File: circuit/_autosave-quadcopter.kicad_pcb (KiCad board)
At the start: 4 copper layers, 37.7 x 37.7 mm, 112 parts, among them J1 Conn_01x01_Female, J10 Conn_01x01_Female, J11 Conn_01x01_Female, J12 Conn_01x01_Female, J13 Conn_01x01_Female, J14 Conn_01x01_Female, J15 Conn_01x01_Female, J16 Conn_01x01_Female, J17 Conn_01x01_Female, J18 USB_C_Receptacle_USB2.0, J19 Conn_01x08_Male, J2 Conn_01x01_Female, J20 Conn_01x04_Male, J21 Conn_01x01_Female, J22 Conn_01x01_Female, J23 Conn_01x01_Female, J24 Conn_01x01_Female, J25 Conn_01x01_Female, J26 Conn_01x01_Female, J27 Conn_01x01_Female, J28 Conn_01x01_Female, J29 Conn_01x01_Female, J3 Conn_01x01_Female, J30 Conn_01x01_Female, J31 Conn_01x01_Female, J32 Conn_01x01_Female, J33 Conn_01x01_Female, J34 Conn_01x01_Female, J35 Conn_01x01_Female, J36 Conn_01x01_Female, J37 Conn_01x01_Female, J38 Conn_01x01_Female, J39 Conn_01x01_Female, J4 Conn_01x01_Female, J40 Conn_01x01_Female, J41 Conn_01x01_Female, J42 Conn_01x01_Female, J43 Conn_01x01_Female, J44 Conn_01x01_Female, J45 Conn_01x01_Female, J46 Conn_01x01_Female, J47 Conn_01x01_Female, J48 Conn_01x01_Female, J49 Conn_01x01_Female, J5 Conn_01x01_Female, J50 Conn_01x01_Female, J51 Conn_01x01_Female, J6 Conn_01x01_Female, J7 Conn_01x01_Female, J8 Conn_01x01_Female, J9 Conn_01x01_Female, SW1 SW_DIP_x01, U1 STM32G431CBU6, U2 ICM-42605, U3 DPS310, U4 3V3, U5 5V, U6 AT7456E, U7 W25Q128JVS, Y1 16M, Y2 27M

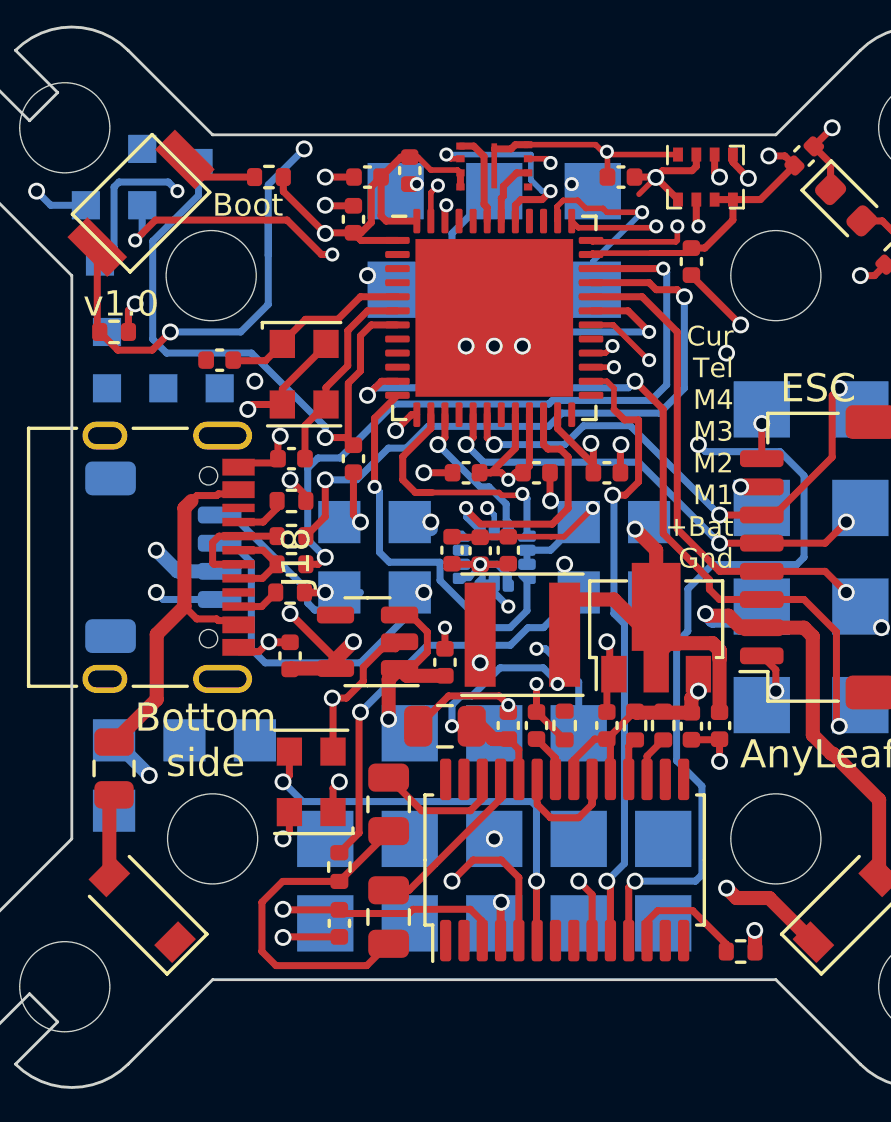
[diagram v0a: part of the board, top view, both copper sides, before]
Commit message: Added CRSF module for radio siganls
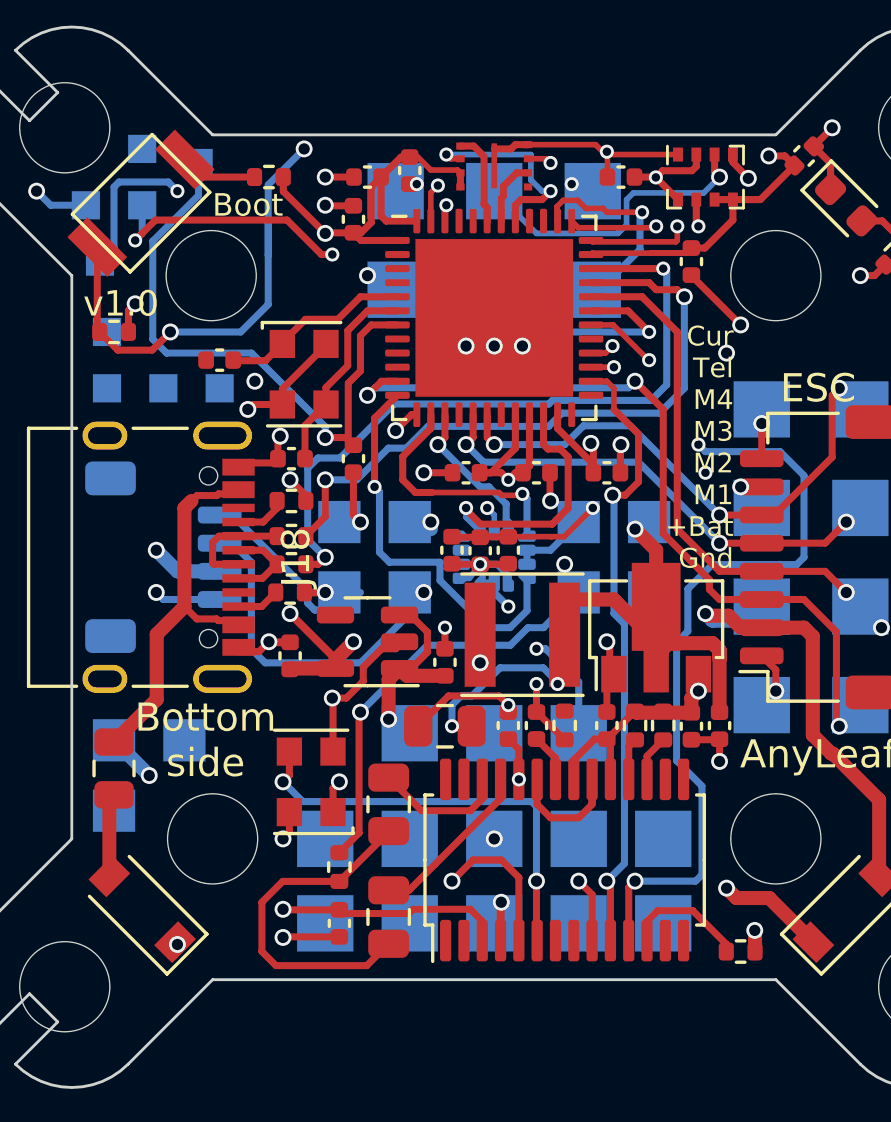
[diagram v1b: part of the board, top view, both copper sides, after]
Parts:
- removed J35: Conn_01x01_Female, TestPoint:TestPoint_Pad_1.5x1.5mm
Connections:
- U1 pad 10: unconnected-(U1-Pad10) -> /UART2_TX
- U1 pad 24: unconnected-(U1-Pad24) -> /UART3_RX
- U1 pad 29: unconnected-(U1-Pad29) -> /BUZZER+
- U1 pad 39: unconnected-(U1-Pad39) -> /UART4_TX
- U1 pad 40: unconnected-(U1-Pad40) -> /UART4_RX
- U1 pad 44: unconnected-(U1-Pad44) -> /UART1_TX
- U1 pad 45: unconnected-(U1-Pad45) -> /UART1_RX
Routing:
- net /MOSI_2: track 8.97 -> 26.4 mm, vias 2 -> 3
- net +5V: track 28.8 -> 27.2 mm, vias 6 -> 8
- net /SDA2: track 20.3 -> 21.4 mm
- net +3V3: track 67.6 -> 66.8 mm
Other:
- board text removed: "Bz-"

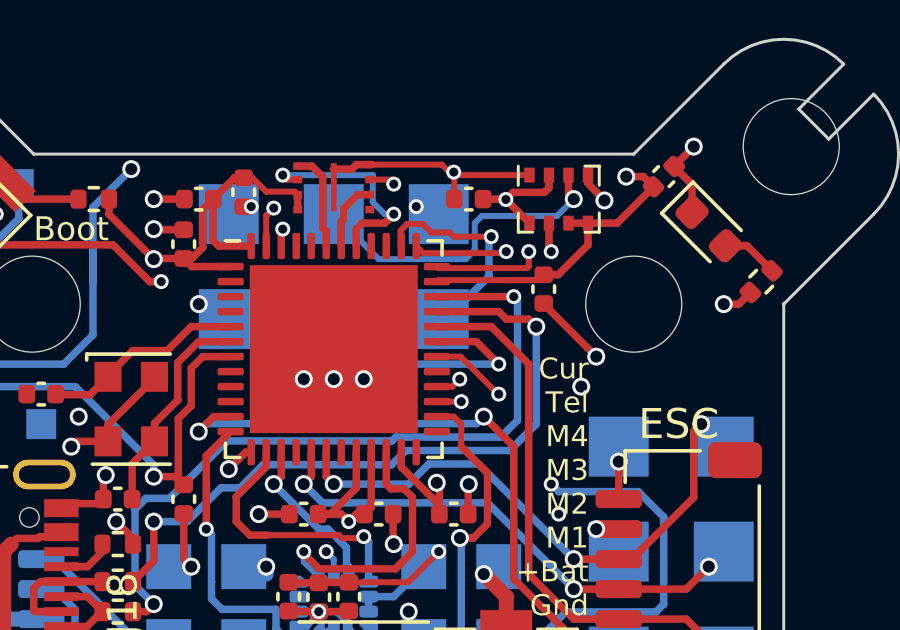
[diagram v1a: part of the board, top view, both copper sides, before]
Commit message: more work on CRSF radio comms
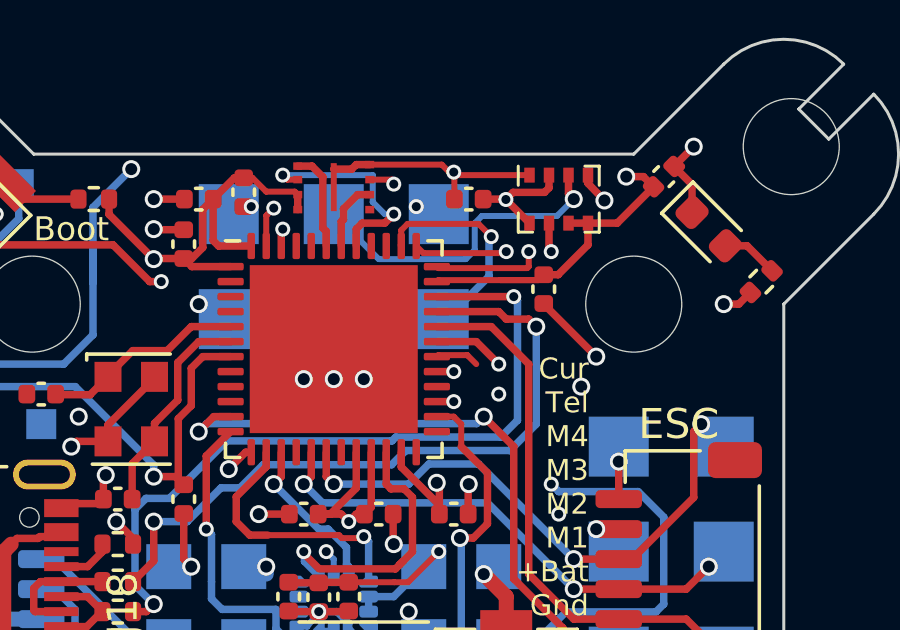
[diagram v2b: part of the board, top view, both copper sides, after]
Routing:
- net /SCL2: track 19.5 -> 16.2 mm
- net /MOSI_2: track 26.4 -> 23.7 mm, vias 3 -> 2
- net /SDA2: track 21.4 -> 20.3 mm
- net /BUZZER+: track 0.00 -> 0.56 mm, vias 0 -> 1
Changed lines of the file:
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@@
       (net 78 "/BUZZER+") (pinfunction "PC6") (pintype "bidirectional") (solder_mask_margin 0.1) (clearance 0.1))
     (pad "30" smd roundrect locked (at 3.4375 0.25) (size 0.875 0.25) (layers "F.Cu" "F.Paste" "F.Mask") (roundrect_rratio 0.25)
-      (net 41 "/SDA2") (pinfunction "PA8") (pintype "bidirectional"))
+      (net 41 "/SDA2") (pinfunction "PA8") (pintype "bidirectional") (solder_mask_margin 0.1) (clearance 0.1))
     (pad "31" smd roundrect locked (at 3.4375 -0.25) (size 0.875 0.25) (layers "F.Cu" "F.Paste" "F.Mask") (roundrect_rratio 0.25)
       (net 40 "/SCL2") (pinfunction "PA9") (pintype "bidirectional"))
@@
   (segment (start 146.022843 74.045175) (end 146.022843 75.684762) (width 0.25) (layer "In2.Cu") (net 40))
   (segment (start 137.75 78) (end 137 78) (width 0.25) (layer "B.Cu") (net 40))
-  (segment (start 142.5 79.5) (end 139.25 79.5) (width 0.25) (layer "B.Cu") (net 40))
   (segment (start 139.25 79.5) (end 137.75 78) (width 0.25) (layer "B.Cu") (net 40))
-  (segment (start 140.4375 79.25) (end 141.227127 79.25) (width 0.2) (layer "F.Cu") (net 41))
-  (segment (start 141.227127 79.25) (end 142.477127 80.5) (width 0.2) (layer "F.Cu") (net 41))
+  (segment (start 140.4375 79.25) (end 140.487011 79.200489) (width 0.2) (layer "F.Cu") (net 41))
+  (segment (start 141.450489 79.200489) (end 141.75 79.5) (width 0.2) (layer "F.Cu") (net 41))
   (segment (start 144.825 73.2) (end 144.825 73.825) (width 0.25) (layer "F.Cu") (net 41))
+  (segment (start 140.487011 79.200489) (end 141.450489 79.200489) (width 0.2) (layer "F.Cu") (net 41))
   (segment (start 142.477127 80.5) (end 142.5 80.5) (width 0.2) (layer "F.Cu") (net 41))
   (segment (start 144.825 73.825) (end 145 74) (width 0.25) (layer "F.Cu") (net 41))
@@
   (segment (start 146 89.75) (end 146.5 89.25) (width 0.5) (layer "B.Cu") (net 46))
   (segment (start 144.5 89.5) (end 144.75 89.75) (width 0.5) (layer "B.Cu") (net 46))
-  (segment (start 139.451647 74.82548) (end 139.962453 74.82548) (width 0.2) (layer "F.Cu") (net 47))
-  (segment (start 140.25 75.113027) (end 140.863027 75.113027) (width 0.2) (layer "F.Cu") (net 47))
-  (segment (start 140.863027 75.113027) (end 141 75.25) (width 0.2) (layer "F.Cu") (net 47))
-  (segment (start 141 75.25) (end 142.25 75.25) (width 0.2) (layer "F.Cu") (net 47))
-  (segment (start 139.227616 75.540116) (end 139.227616 75.049511) (width 0.2) (layer "F.Cu") (net 47))
+  (segment (start 139.25 75.037547) (end 139.25 75.5625) (width 0.2) (layer "F.Cu") (net 47))
+  (segment (start 141.82548 74.82548) (end 139.462067 74.82548) (width 0.2) (layer "F.Cu") (net 47))
+  (segment (start 142.25 75.25) (end 141.82548 74.82548) (width 0.2) (layer "F.Cu") (net 47))
   (segment (start 139.25 75.5625) (end 139.227616 75.540116) (width 0.2) (layer "F.Cu") (net 47))
-  (segment (start 139.962453 74.82548) (end 140.25 75.113027) (width 0.2) (layer "F.Cu") (net 47))
-  (segment (start 139.227616 75.049511) (end 139.451647 74.82548) (width 0.2) (layer "F.Cu") (net 47))
+  (segment (start 139.462067 74.82548) (end 139.25 75.037547) (width 0.2) (layer "F.Cu") (net 47))
   (via (at 142.25 75.25) (size 0.5) (drill 0.3) (layers "F.Cu" "B.Cu") (free) (net 47))
   (segment (start 142.175489 76.574511) (end 140.75 78) (width 0.25) (layer "B.Cu") (net 47))
@@
   (segment (start 123.5 76.5) (end 123 77) (width 0.25) (layer "B.Cu") (net 77))
   (segment (start 125.425489 74.175489) (end 123.675489 74.175489) (width 0.25) (layer "B.Cu") (net 77))
+  (segment (start 140.4375 79.75) (end 141 79.75) (width 0.2) (layer "F.Cu") (net 78))
+  (via (at 141 79.75) (size 0.5) (drill 0.3) (layers "F.Cu" "B.Cu") (net 78))
   (segment (start 140.475 99.475) (end 140 99) (width 0.25) (layer "F.Cu") (net 79))
-  (segment (start 140.95 80.25) (end 141.2 80) (width 0.2) (layer "F.Cu") (net 79))
-  (segment (start 140.4375 80.25) (end 140.95 80.25) (width 0.2) (layer "F.Cu") (net 79))
   (segment (start 140.475 101.1125) (end 140.475 99.475) (width 0.25) (layer "F.Cu") (net 79))
   (via (at 144.5 84.5) (size 0.5) (drill 0.3) (layers "F.Cu" "B.Cu") (free) (net 79))
-  (via (at 141.2 80) (size 0.5) (drill 0.3) (layers "F.Cu" "B.Cu") (free) (net 79))
   (via (at 140 99) (size 0.6) (drill 0.4) (layers "F.Cu" "B.Cu") (net 79))
   (segment (start 144.5 84.883193) (end 140 89.383193) (width 0.25) (layer "In1.Cu") (net 79))
@@
   (segment (start 140 89.383193) (end 140 99) (width 0.25) (layer "In1.Cu") (net 79))
   (segment (start 143.5 84.5) (end 144.5 84.5) (width 0.25) (layer "In2.Cu") (net 79))
-  (segment (start 141.2 80) (end 141.187518 80) (width 0.25) (layer "In2.Cu") (net 79))
   (segment (start 140.675489 81.675489) (end 143.5 84.5) (width 0.25) (layer "In2.Cu") (net 79))
-  (segment (start 141.187518 80) (end 140.675489 80.512029) (width 0.25) (layer "In2.Cu") (net 79))
-  (segment (start 140.675489 80.512029) (end 140.675489 81.675489) (width 0.25) (layer "In2.Cu") (net 79))
   (segment (start 141.125 99.125) (end 141 99) (width 0.25) (layer "F.Cu") (net 80))
   (segment (start 141.125 101.1125) (end 141.125 99.125) (width 0.25) (layer "F.Cu") (net 80))
@@
   (segment (start 141.25 89.5) (end 141.25 85.250809) (width 0.25) (layer "B.Cu") (net 80))
   (segment (start 141.624511 89.874511) (end 141.25 89.5) (width 0.25) (layer "B.Cu") (net 80))
-  (segment (start 140.4375 80.75) (end 141.25 80.75) (width 0.2) (layer "F.Cu") (net 81))
+  (segment (start 140.4375 80.75) (end 141 80.75) (width 0.2) (layer "F.Cu") (net 81))
   (segment (start 141.775 101.1125) (end 141.775 99.225) (width 0.25) (layer "F.Cu") (net 81))
   (segment (start 141.775 99.225) (end 142 99) (width 0.25) (layer "F.Cu") (net 81))
-  (via (at 141.25 80.75) (size 0.5) (drill 0.3) (layers "F.Cu" "B.Cu") (free) (net 81))
+  (via (at 141 80.75) (size 0.5) (drill 0.3) (layers "F.Cu" "B.Cu") (free) (net 81))
   (via (at 144.25 83.5) (size 0.5) (drill 0.3) (layers "F.Cu" "B.Cu") (net 81))
   (via (at 142 99) (size 0.6) (drill 0.4) (layers "F.Cu" "B.Cu") (net 81))
-  (segment (start 141.25 81.383193) (end 141.25 80.75) (width 0.25) (layer "In2.Cu") (net 81))
+  (segment (start 141.375489 81.125489) (end 141 80.75) (width 0.25) (layer "In2.Cu") (net 81))
+  (segment (start 143.366807 83.5) (end 141.375489 81.508682) (width 0.25) (layer "In2.Cu") (net 81))
   (segment (start 144.25 83.5) (end 143.366807 83.5) (width 0.25) (layer "In2.Cu") (net 81))
-  (segment (start 143.366807 83.5) (end 141.25 81.383193) (width 0.25) (layer "In2.Cu") (net 81))
+  (segment (start 141.375489 81.508682) (end 141.375489 81.125489) (width 0.25) (layer "In2.Cu") (net 81))
   (segment (start 143.875489 88.624511) (end 144.741318 87.758682) (width 0.25) (layer "B.Cu") (net 81))
   (segment (start 147.149022 83.75) (end 144.5 83.75) (width 0.25) (layer "B.Cu") (net 81))

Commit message: Updated pin assignments
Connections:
- net /M1_PWM renamed /M1
- net /M2_PWM renamed /M2
- net /M3_PWM renamed /M3
- net /M4_PWM renamed /M4
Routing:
- net GND: vias 32 -> 31

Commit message: More work on routing
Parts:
- moved J50 2.91 mm to (137.2, 71.6)
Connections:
- U1 pad 11: /M1 -> /UART2_RX
- U1 pad 22: /CS_IMU -> /UART3_TX
- U1 pad 8: unconnected-(U1-Pad8) -> /M1
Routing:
- net /UART4_TX: track 0.00 -> 31.8 mm, vias 0 -> 2
- net /UART4_RX: track 0.00 -> 28.9 mm, vias 0 -> 2
- net /UART1_TX: track 0.00 -> 17.2 mm, vias 0 -> 2
- net /UART1_RX: track 0.00 -> 12.5 mm, vias 0 -> 1
- net /CS_IMU: track 9.23 -> 1.11 mm
- net /SCK_3: track 7.38 -> 4.50 mm
- net /UART2_RX: track 0.00 -> 1.27 mm, vias 0 -> 1
- net /SDA1: track 7.11 -> 8.06 mm
- net /SDA2: track 20.3 -> 19.3 mm
- net /M1: track 28.5 -> 27.9 mm
- net /MOSI_2: track 23.7 -> 24.2 mm
- net (no net): track 0.00 -> 0.10 mm, vias 0 -> 1

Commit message: More work on CRSF
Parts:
- J50: footprint TestPoint:TestPoint_Pad_2.0x2.0mm -> TestPoint:TestPoint_Pad_1.0x1.0mm
- moved J50 2.21 mm to (137.0, 73.8)
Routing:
- net /UART3_RX: track 0.00 -> 48.9 mm, vias 0 -> 1
- net /UART1_RX: track 12.5 -> 52.6 mm, vias 1 -> 2
- net /UART1_TX: track 17.2 -> 53.8 mm, vias 2 -> 5
- net /UART2_TX: track 0.00 -> 34.3 mm, vias 0 -> 2
- net GND: track 69.0 -> 103.1 mm
- net /UART2_RX: track 1.27 -> 28.7 mm, vias 1 -> 2
- net /UART3_TX: track 0.00 -> 25.0 mm, vias 0 -> 2
- net /SWDIO: track 29.1 -> 8.98 mm
- net +5V: track 27.6 -> 46.3 mm
- net /SWCLK: track 24.3 -> 12.5 mm, vias 3 -> 2
- net +3V3: track 66.8 -> 76.5 mm, vias 13 -> 12
- net /SCK_2: track 22.1 -> 25.1 mm
- net /SDA2: track 19.3 -> 22.3 mm
- net Net-(D2-Pad1): track 18.3 -> 20.3 mm
- net /UART4_RX: track 28.9 -> 29.8 mm
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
